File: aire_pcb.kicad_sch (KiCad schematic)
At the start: 55 parts, among them J1 Conn_01x02_Male, J2 Screw_Terminal_01x02, J3 Screw_Terminal_01x03, J4 Conn_01x04_Male, J5 Conn_02x04_Top_Bottom, K1 JRC-21F_4100, K2 JRC-21F_4100, K3 JRC-21F_4100, Q1 2N3904, Q2 2N3904, Q3 2N3904, SW1 SW_Push, SW2 SW_Push, U1 NCP1117-3.3_SOT223, U2 HLK-2M05, U3 SHT40, U4 ESP8266-12E{slash}ESP-12E

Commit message: Change transistors and diodes to SMD
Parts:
- added F2: Fuse, guille_3rdparty:Fuse_2512_6332Metric, symbol Device:Fuse
- D2, D4, D6: footprint Diode_THT:D_A-405_P7.62mm_Horizontal -> Diode_SMD:D_SOD-323
- Q1, Q2, Q3: footprint Package_TO_SOT_THT:TO-92_Inline -> Package_TO_SOT_SMD:SOT-23
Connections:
- net +5V: now also C1.1, J1.1 (Pin_1), U1.3 (VI); no longer J1.2 (Pin_2), U2.4 (V+)
- net FAN1: now also U4.7 (IO13); no longer U4.6 (IO12)
- net FAN2: now also U4.6 (IO12); no longer U4.7 (IO13)
- net L: no longer K1.1 (COM_1), K1.6 (COM_2), K2.1 (COM_1), K2.6 (COM_2), K3.1 (COM_1), K3.6 (COM_2)
- net at F1.2, RV1.1, U2.1 (AC/L): now also F2.1
- new net: J1.2 (Pin_2), U2.4 (V+)
- new net LF: F2.2, K1.1 (COM_1), K1.6 (COM_2), K2.1 (COM_1), K2.6 (COM_2), K3.1 (COM_1), K3.6 (COM_2)
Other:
- note added: "Revisar FUSES"
- note removed: "FUSES?"
- moved on the sheet: J1

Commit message: Minor redesign
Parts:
- removed F2: Fuse, guille_3rdparty:Fuse_2512_6332Metric, symbol Device:Fuse
- removed J1: Conn_01x02_Male, Connector_PinHeader_2.54mm:PinHeader_1x02_P2.54mm_Vertical, symbol Connector:Conn_01x02_Male
- removed J4: Conn_01x04_Male, Connector_PinHeader_2.54mm:PinHeader_1x04_P2.54mm_Vertical, symbol Connector:Conn_01x04_Male
- removed U1: NCP1117-3.3_SOT223, Package_TO_SOT_SMD:SOT-223-3_TabPin2, symbol Regulator_Linear:NCP1117-3.3_SOT223
- added C6: 100n, Capacitor_SMD:C_0402_1005Metric, symbol Device:C
- added J1: Conn_01x04_Pin, Connector_PinHeader_2.54mm:PinHeader_1x04_P2.54mm_Vertical, symbol Connector:Conn_01x04_Pin
- added J6: Conn_01x03_Socket, Connector_PinSocket_2.54mm:PinSocket_1x03_P2.54mm_Vertical, symbol Connector:Conn_01x03_Socket
- added J7: Conn_01x02_Pin, Connector_PinHeader_2.54mm:PinHeader_1x02_P2.54mm_Vertical, symbol Connector:Conn_01x02_Pin
- added U5: NCP1117-3.3_SOT223, Package_TO_SOT_SMD:SOT-223-3_TabPin2, symbol Regulator_Linear:NCP1117-3.3_SOT223
- H1, H2, H3, H4: footprint MountingHole:MountingHole_3.2mm_M3_DIN965 -> MountingHole:MountingHole_3.2mm_M3_Pad_TopBottom; symbol Mechanical:MountingHole -> Mechanical:MountingHole_Pad
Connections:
- net +3V3: now also J1.1 (Pin_1), U5.2 (VO)
- net +5V: now also C6.1, J6.3 (Pin_3), J7.1 (Pin_1), U5.3 (VI)
- net GND: now also C6.2, J1.4 (Pin_4), J6.1 (Pin_1), U5.1 (GND)
- net LF: now also F1.2, RV1.1, U2.1 (AC/L)
- net RX: now also J1.3 (Pin_3)
- net TX: now also J1.2 (Pin_2)
- net at U2.4 (V+): now also J7.2 (Pin_2)
- net EXT2 renamed TEMP
- net TEMP: now also J6.2 (Pin_2)
- no-connect marks 3 -> 7
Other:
- note added: "Microcontroller"
- note added: "Other external connectors"
- note added: "Power supply"
- note added: "Relays"
- note added: "Sensors and actuators"
- note removed: "Revisar FUSES"
- moved on the sheet: BZ1, C1, C2, C3, C4, D1, D2, D3, D4, D5, D6, D7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

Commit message: PCB changes
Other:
- note added: "MEJORAS: - Revisar diametro holes - Juntar más los relés? - Pistas de potencia más anchas - Maristor está encima de HiLink - Revisar clearance pistas de potencia - Mover condensador temp ext - C1 muy cerca del HiLink - Pads reles muy pequeños - Transistor al revés - Buzzer con transistor - Pinouts de lso transistores mal (base y esmisor cambiados) - TP en vex de header para programar - Juntar más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"
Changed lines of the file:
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@@
     (effects (font (size 2.54 2.54) (thickness 0.508) bold) (justify left bottom))
+  )
+  (text "MEJORAS:\n- Revisar diametro holes\n- Juntar más los relés?\n- Pistas de potencia más anchas\n- Maristor está encima de HiLink\n- Revisar clearance pistas de potencia\n- Mover condensador temp ext\n- C1 muy cerca del HiLink\n- Pads reles muy pequeños\n- Transistor al revés\n- Buzzer con transistor\n- Pinouts de lso transistores mal (base y esmisor cambiados)\n- TP en vex de header para programar\n- Juntar más relés\n- SMD en una capa, TH en otra\n- Reles fríos\n- PIN IO13 parpadea cuando no se ha configurado el WiFi. Cambiar a otro y poner un LED?"
+    (at 67.31 196.85 0)
+    (effects (font (size 1.27 1.27)) (justify left bottom))
   )
   (text "Sensors and actuators" (at 139.7 123.19 0)

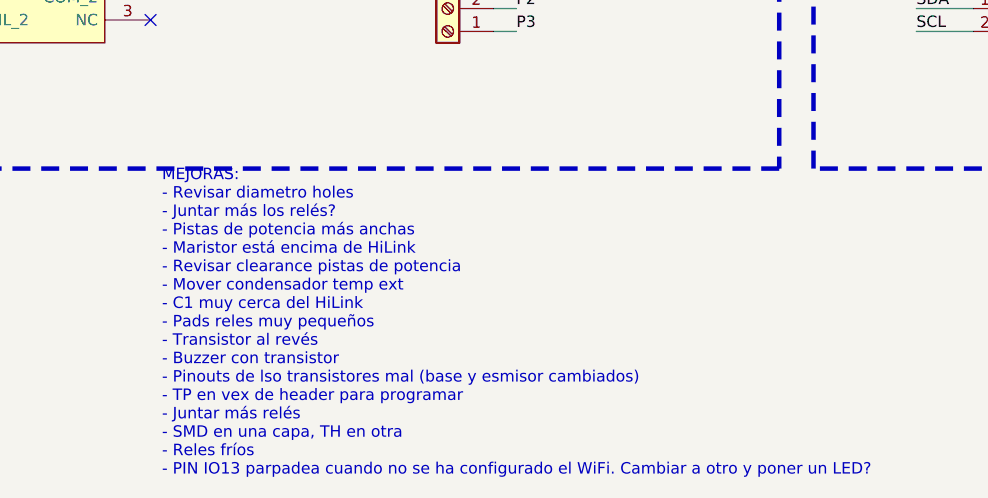
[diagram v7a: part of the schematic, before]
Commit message: Add GIT library
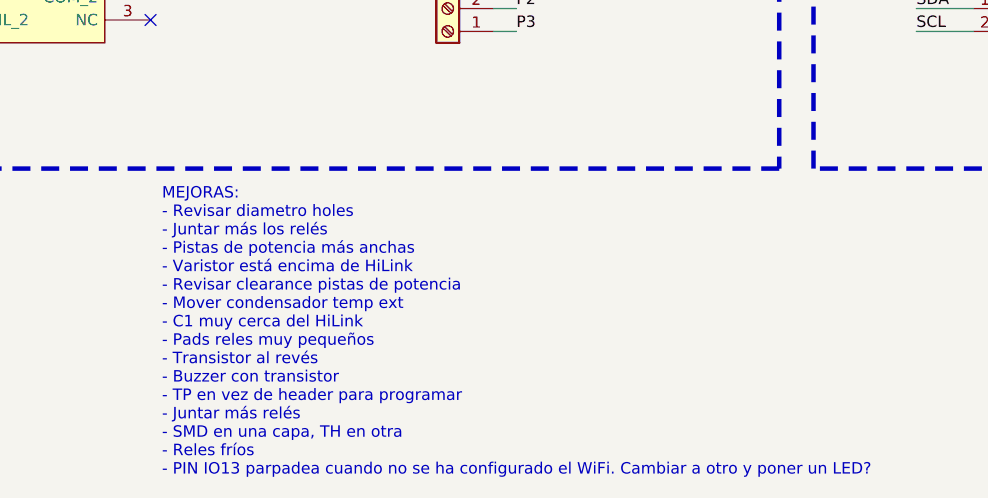
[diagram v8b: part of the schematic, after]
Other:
- note added: "MEJORAS: - Revisar diametro holes - Juntar más los relés - Pistas de potencia más anchas - Varistor está encima de HiLink - Revisar clearance pistas de potencia - Mover condensador temp ext - C1 muy cerca del HiLink - Pads reles muy pequeños - Transistor al revés - Buzzer con transistor - TP en vez de header para programar - Juntar más relés - SMD en una capa, TH en otra - Reles fríos - PIN IO13 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"
- note removed: "MEJORAS: - Revisar diametro holes - Juntar más los relés? - Pistas de potencia más anchas - Maristor está encima de HiLink - Revisar clearance pistas de potencia - Mover condensador temp ext - C1 muy cerca del HiLink - Pads reles muy pequeños - Transistor al revés - Buzzer con transistor - Pinouts de lso transistores mal (base y esmisor cambiados) - TP en vex de header para programar - Juntar más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"
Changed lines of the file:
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@@
     (date "2022-08-31")
     (company "Guille")
-    (comment 1 "On every boot/reset/wake, GPIO15 muest be LOW, GPIO2 mst be HIGH")
+    (comment 1 "On every boot/reset/wake, GPIO15 must be LOW, GPIO2 must be HIGH")
     (comment 2 "Run mode: GPIO0 HIGH. Flash mode GPIO0 LOW ")
   )
@@
     (effects (font (size 2.54 2.54) (thickness 0.508) bold) (justify left bottom))
   )
-  (text "MEJORAS:\n- Revisar diametro holes\n- Juntar más los relés?\n- Pistas de potencia más anchas\n- Maristor está encima de HiLink\n- Revisar clearance pistas de potencia\n- Mover condensador temp ext\n- C1 muy cerca del HiLink\n- Pads reles muy pequeños\n- Transistor al revés\n- Buzzer con transistor\n- Pinouts de lso transistores mal (base y esmisor cambiados)\n- TP en vex de header para programar\n- Juntar más relés\n- SMD en una capa, TH en otra\n- Reles fríos\n- PIN IO13 parpadea cuando no se ha configurado el WiFi. Cambiar a otro y poner un LED?"
+  (text "MEJORAS:\n- Revisar diametro holes\n- Juntar más los relés\n- Pistas de potencia más anchas\n- Varistor está encima de HiLink\n- Revisar clearance pistas de potencia\n- Mover condensador temp ext\n- C1 muy cerca del HiLink\n- Pads reles muy pequeños\n- Transistor al revés\n- Buzzer con transistor\n- TP en vez de header para programar\n- Juntar más relés\n- SMD en una capa, TH en otra\n- Reles fríos\n- PIN IO13 parpadea cuando no se ha configurado el WiFi. Cambiar a otro y poner un LED?"
     (at 67.31 196.85 0)
     (effects (font (size 1.27 1.27)) (justify left bottom))
